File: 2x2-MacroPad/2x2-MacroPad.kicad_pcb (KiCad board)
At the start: 2 copper layers, 72.6 x 38.1 mm, 24 parts, among them SW1 SW_Push, U1 ATmega32U4-A, Y1 16MHz

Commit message: Routed everything except keys
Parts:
- moved C3 9.28 mm to (82.5, 63.5), turned to 180 degrees
- moved F1 7.94 mm to (77.6, 49.3)
- moved R4 7.10 mm to (84.0, 50.9), turned to -90 degrees
- moved C1 4.33 mm to (83.2, 58.9)
- moved C5 3.35 mm to (84.0, 56.5)
- moved R2 3.27 mm to (81.0, 42.1)
- moved R3 2.51 mm to (78.6, 42.1)
- moved C6 2.50 mm to (96.3, 68.3)
- moved C7 2.35 mm to (86.5, 46.8)
- moved C4 2.34 mm to (96.7, 46.8)
- moved Y1 2.34 mm to (91.6, 46.8)
- moved SW1 1.77 mm to (76.2, 66.7), turned to 180 degrees
- moved U1 1.58 mm to (92.8, 59.4)
- moved C2 1.25 mm to (101.6, 55.6)
- moved R1 0.70 mm to (101.6, 65.1)
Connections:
- USB1 pad 3: D- -> D+
- USB1 pad 4: D+ -> D-
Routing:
- net GND: track 0.00 -> 107.2 mm
- net +5V: track 0.00 -> 92.6 mm, vias 0 -> 5
- net Net-(U1-D-): track 0.00 -> 25.6 mm
- net Net-(U1-D+): track 0.00 -> 24.6 mm
- net Net-(U1-~{RESET}): track 0.00 -> 23.8 mm, vias 0 -> 2
- net VCC: track 0.00 -> 10.8 mm
- net Net-(U1-XTAL1): track 0.00 -> 9.49 mm
- net Net-(U1-XTAL2): track 0.00 -> 3.69 mm
- net Net-(U1-~{HWB}/PE2): track 0.00 -> 3.38 mm
- net Net-(U1-UCAP): track 0.00 -> 3.25 mm
- net D-: track 4.59 -> 3.44 mm
- net D+: track 4.56 -> 3.80 mm

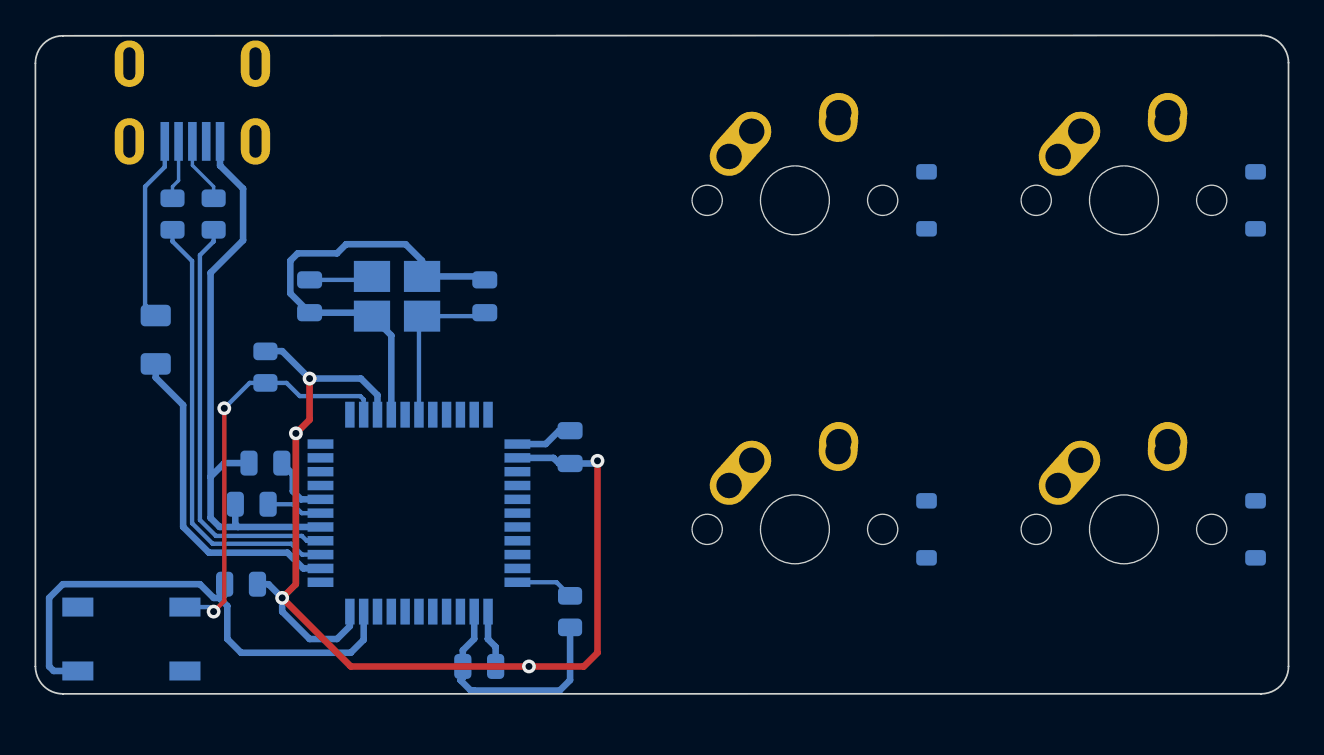
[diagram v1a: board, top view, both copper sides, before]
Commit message: Finished Routing
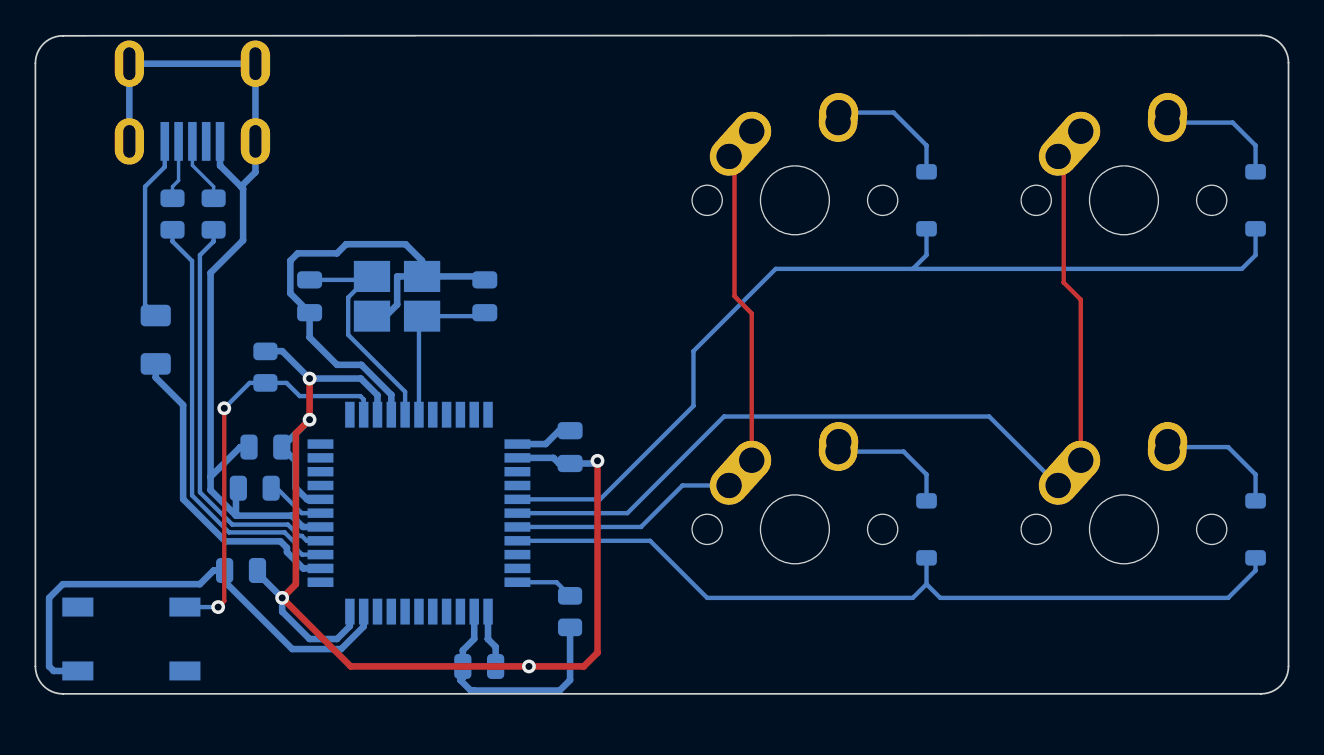
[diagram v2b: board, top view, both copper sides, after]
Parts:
- moved C1 0.94 mm to (83.3, 57.9)
- moved C5 0.93 mm to (84.0, 55.6)
- moved C3 0.79 mm to (82.5, 62.7)
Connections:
- U1 pad 27: unconnected-(U1-PD7-Pad27) -> ROW0
- U1 pad 28: unconnected-(U1-PB4-Pad28) -> COL1
- U1 pad 29: unconnected-(U1-PB5-Pad29) -> COL0
- U1 pad 30: unconnected-(U1-PB6-Pad30) -> ROW1
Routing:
- net ROW0: track 0.00 -> 54.6 mm
- net COL1: track 0.00 -> 53.9 mm
- net ROW1: track 0.00 -> 47.7 mm
- net COL0: track 0.00 -> 31.4 mm
- net GND: track 107.2 -> 128.8 mm
- net Net-(U1-XTAL2): track 3.69 -> 13.7 mm
- net Net-(D4-A): track 0.00 -> 7.41 mm
- net Net-(D1-A): track 0.00 -> 7.39 mm
- net Net-(D2-A): track 0.00 -> 7.19 mm
- net Net-(D3-A): track 0.00 -> 7.19 mm
- net +5V: track 92.6 -> 95.2 mm
- net Net-(U1-D+): track 24.6 -> 23.7 mm
- net Net-(U1-D-): track 25.6 -> 24.9 mm

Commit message: Finished
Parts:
- moved C7 2.38 mm to (88.9, 46.8)
- moved Y1 2.08 mm to (93.7, 46.8)
- moved C4 1.77 mm to (98.4, 46.8)
- moved C3 0.79 mm to (82.5, 63.5)
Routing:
- net GND: track 128.8 -> 107.6 mm
- net +5V: track 95.2 -> 101.7 mm
- net Net-(U1-XTAL2): track 13.7 -> 9.91 mm
- net Net-(U1-D+): track 23.7 -> 24.6 mm
- net Net-(U1-XTAL1): track 9.49 -> 10.0 mm
- added copper zone on B.Cu, net (none)
- added copper zone on B.Cu, net GND
